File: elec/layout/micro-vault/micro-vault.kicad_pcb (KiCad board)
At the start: 2 copper layers, 28 x 20 mm, 32 parts

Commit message: checkin
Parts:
- added R16: 10kΩ ±1% 62.5mW, atopile:R0402-56259e, F.Cu at (0.00, 0.00)
- added R17: 10kΩ ±1% 62.5mW, atopile:R0402-56259e, F.Cu at (0.00, -10.0)
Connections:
- C1 pad 1: hv -> hv-3
- C2 pad 1: hv -> hv-3
- C3 pad 1: hv-1 -> hv
- C4 pad 1: hv-1 -> hv
- C8 pad 1: hv-3 -> hv-1
- C9 pad 1: hv-1 -> hv
- R11 pad 1: hv-1 -> hv
- R12 pad 1: heater_controller-net-3 -> heater_controller-net-6
- R12 pad 2: heater_controller-net-2 -> heater_controller-net-4
- R13 pad 1: heater_controller-net-2 -> heater_controller-net-4
- R14 pad 2: heater_controller-net-6 -> heater_controller-net-5
- R15 pad 1: heater_controller-net-6 -> heater_controller-net-5
- R2 pad 1: hv-3 -> hv-1
- R2 pad 2: heater_controller-net-4 -> heater_controller-net-1
- R3 pad 1: heater_controller-net-4 -> heater_controller-net-1
- R3 pad 2: heater_controller-net-1 -> heater_controller-net-3
- R4 pad 1: heater_controller-net-1 -> heater_controller-net-3
- R4 pad 2: heater_controller-net-5 -> heater_controller-net-2
- R5 pad 1: heater_controller-net-5 -> heater_controller-net-2
- R5 pad 2: heater_controller-net-3 -> heater_controller-net-6
- R9 pad 1: hv-1 -> hv
- U2 pad 1: hv -> hv-3
- U2 pad 2: hv-1 -> hv
- U3 pad 12: hv -> hv-3
- U3 pad 13: hv-1 -> hv
- U3 pad 3: hv-1 -> hv
- U6 pad 2: hv-1 -> hv
- U7 pad 1: hv-3 -> hv-1
- U7 pad 3: hv-3 -> hv-1
- U7 pad 5: hv-1 -> hv
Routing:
- net (no net): track 0.00 -> 58.2 mm, vias 0 -> 6
- net hv: track 7.33 -> 51.8 mm, vias 2 -> 6
- net hv-1: track 51.8 -> 20.6 mm, vias 6 -> 2
- net SCL: track 21.2 -> 0.00 mm, vias 2 -> 0
- net SDA: track 19.5 -> 0.00 mm, vias 2 -> 0
- net Vplus: track 17.5 -> 0.00 mm, vias 2 -> 0
- net hv-3: track 20.6 -> 7.33 mm
- net heater_controller-net-6: track 9.44 -> 4.25 mm
- net heater_controller-net-1: track 3.62 -> 6.47 mm
- net heater_controller-net-2: track 4.99 -> 7.27 mm
- net heater_controller-net-5: track 7.27 -> 9.44 mm
- net heater_controller-net-4: track 6.47 -> 4.99 mm
- net heater_controller-net-3: track 4.25 -> 3.62 mm

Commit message: checkin
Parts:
- moved R17 165.5 mm to (115.5, 108.5), turned to 180 degrees
- moved R16 159.8 mm to (117.3, 108.5)
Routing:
- net (no net): track 58.2 -> 0.00 mm, vias 6 -> 0
- net Vplus: track 0.00 -> 26.8 mm, vias 0 -> 3
- net SCL: track 0.00 -> 22.8 mm, vias 0 -> 2
- net SDA: track 0.00 -> 21.3 mm, vias 0 -> 2
- net hv-1: track 20.6 -> 21.2 mm

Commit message: build with excluded checks
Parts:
- removed R16, R17: 10kΩ ±1% 62.5mW, atopile:R0402-56259e
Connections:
- C1 pad 1: hv-3 -> hv-1
- C2 pad 1: hv-3 -> hv-1
- C3 pad 1: hv -> hv-2
- C4 pad 1: hv -> hv-2
- C5 pad 1: hv-2 -> hv-3
- C6 pad 1: hv-2 -> hv-3
- C7 pad 1: hv-2 -> hv-3
- C8 pad 1: hv-1 -> hv
- C9 pad 1: hv -> hv-2
- R11 pad 1: hv -> hv-2
- R12 pad 1: heater_controller-net-6 -> heater_controller-net-3
- R12 pad 2: heater_controller-net-4 -> heater_controller-net-1
- R13 pad 1: heater_controller-net-4 -> heater_controller-net-1
- R13 pad 2: heater_controller-net -> heater_controller-net-6
- R14 pad 1: heater_controller-net -> heater_controller-net-6
- R14 pad 2: heater_controller-net-5 -> heater_controller-net-4
- R15 pad 1: heater_controller-net-5 -> heater_controller-net-4
- R2 pad 1: hv-1 -> hv
- R2 pad 2: heater_controller-net-1 -> heater_controller-net
- R3 pad 1: heater_controller-net-1 -> heater_controller-net
- R3 pad 2: heater_controller-net-3 -> heater_controller-net-2
- R4 pad 1: heater_controller-net-3 -> heater_controller-net-2
- R4 pad 2: heater_controller-net-2 -> heater_controller-net-5
- R5 pad 1: heater_controller-net-2 -> heater_controller-net-5
- R5 pad 2: heater_controller-net-6 -> heater_controller-net-3
- R9 pad 1: hv -> hv-2
- U2 pad 1: hv-3 -> hv-1
- U2 pad 2: hv -> hv-2
- U3 pad 12: hv-3 -> hv-1
- U3 pad 13: hv -> hv-2
- U3 pad 3: hv -> hv-2
- U3 pad 8: hv-2 -> hv-3
- U6 pad 2: hv -> hv-2
- U6 pad 6: hv-2 -> hv-3
- U7 pad 1: hv-1 -> hv
- U7 pad 3: hv-1 -> hv
- U7 pad 5: hv -> hv-2
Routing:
- net hv-2: track 20.1 -> 51.8 mm, vias 2 -> 6
- net hv: track 51.8 -> 21.2 mm, vias 6 -> 2
- net hv-1: track 21.2 -> 7.33 mm
- net hv-3: track 7.33 -> 20.1 mm
- net heater_controller-net-6: track 4.25 -> 10.5 mm, vias 0 -> 2
- net heater_controller-net-4: track 4.99 -> 9.44 mm
- net heater_controller-net: track 10.5 -> 6.47 mm, vias 2 -> 0
- net heater_controller-net-2: track 7.27 -> 3.62 mm
- net heater_controller-net-5: track 9.44 -> 7.27 mm
- net heater_controller-net-1: track 6.47 -> 4.99 mm
- net gnd: track 105.9 -> 107.3 mm
- net heater_controller-net-3: track 3.62 -> 4.25 mm

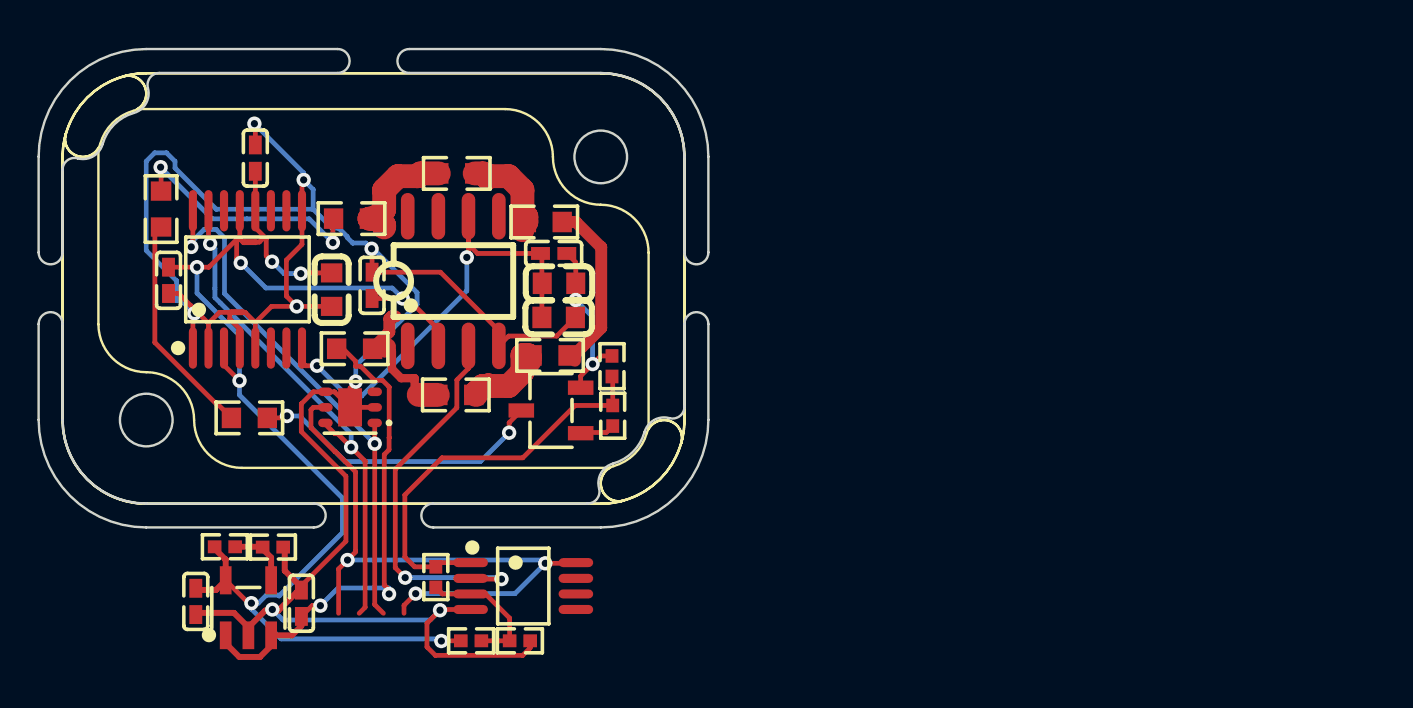
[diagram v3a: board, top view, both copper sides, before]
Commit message: checkin, microvault refactor
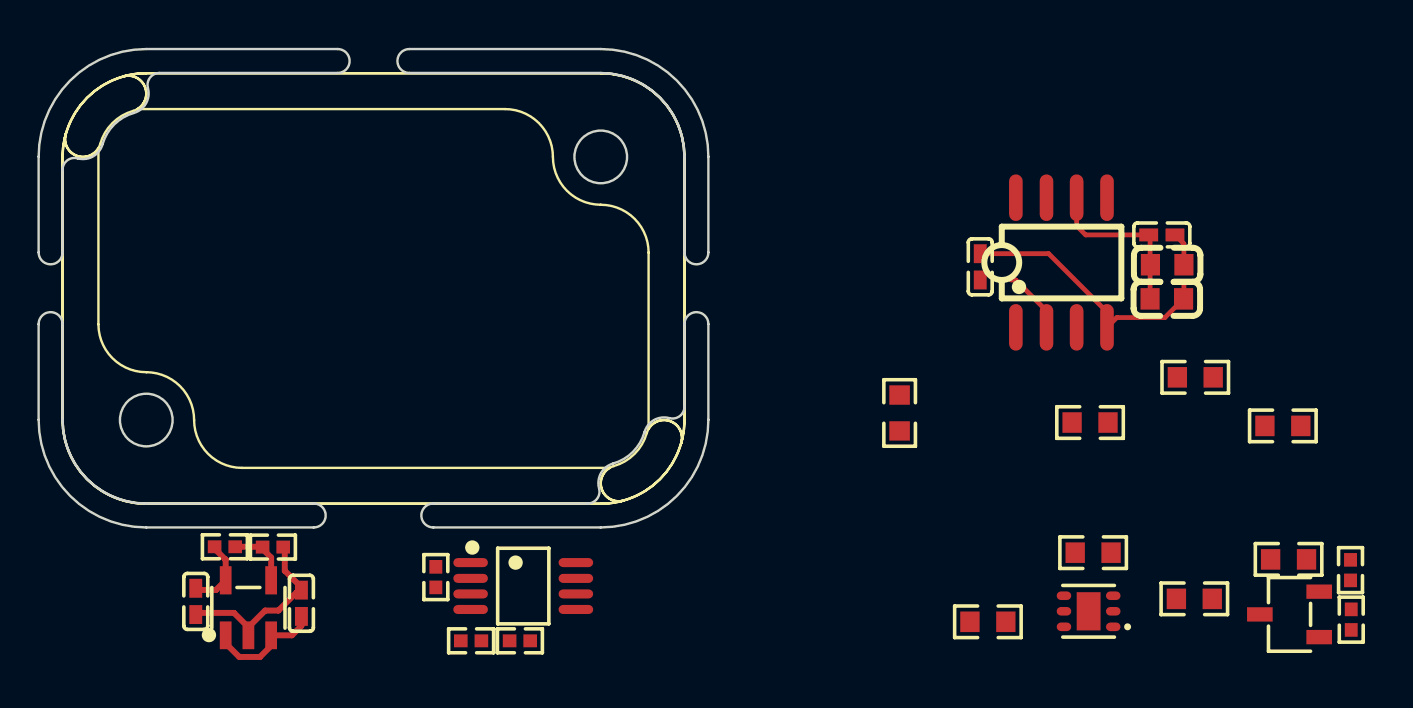
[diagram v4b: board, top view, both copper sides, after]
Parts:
- removed C1, C3: 100nF ±10% 16V X7R, atopile:C0402-b3ef17
- removed C2: 10µF ±10% 10V X5R, atopile:C0603-bd72f6
- removed U1, U2: , lib:NetTie-2_SMD_Pad0.25mm
- removed U3: , atopile:TSSOP-16_L5.0-W4.4-P0.65-LS6.4-BL-4f6acc
- moved R12 32.0 mm to (150.8, 98.7)
- moved R4 32.0 mm to (154.7, 106.3)
- moved Q1 32.0 mm to (154.8, 108.6)
- moved R13 32.0 mm to (146.4, 100.6)
- moved R2 32.0 mm to (146.6, 106.0)
- moved R5 32.0 mm to (154.5, 100.7)
- moved U8 32.0 mm to (146.4, 108.5)
- moved R14 32.0 mm to (138.5, 100.2)
- moved R15 32.0 mm to (142.2, 108.9)
- moved R3 32.0 mm to (150.8, 107.9)
- moved R6 32.0 mm to (157.4, 108.8)
- moved R7 32.0 mm to (157.3, 106.7)
- moved C7 25.4 mm to (149.6, 95.4)
- moved U6 25.4 mm to (145.2, 93.9)
- moved C4 25.4 mm to (141.8, 94.1)
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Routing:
- net gnd: track 107.3 -> 20.5 mm, vias 10 -> 0
- net hv-2: track 51.8 -> 5.76 mm, vias 6 -> 0
- net Vplus: track 26.8 -> 0.00 mm, vias 3 -> 0
- net SCL: track 22.8 -> 0.00 mm, vias 2 -> 0
- net SDA: track 21.3 -> 0.00 mm, vias 2 -> 0
- net OUT1: track 16.8 -> 0.00 mm
- net TEMP: track 16.5 -> 0.00 mm, vias 2 -> 0
- net hv: track 21.2 -> 5.00 mm, vias 2 -> 0
- net hv-3: track 20.1 -> 7.05 mm, vias 2 -> 0
- net heater_controller-gnd: track 12.6 -> 0.00 mm, vias 2 -> 0
- net heater_controller-net-6: track 10.5 -> 0.00 mm, vias 2 -> 0
- net heater_controller-net-4: track 9.44 -> 0.00 mm
- net hv-1: track 7.33 -> 0.00 mm, vias 2 -> 0
- net heater_controller-net-5: track 7.27 -> 0.00 mm
- net heater_controller-net: track 6.47 -> 0.00 mm
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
